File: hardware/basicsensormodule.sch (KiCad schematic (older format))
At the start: 6 parts, among them J1 Conn_01x04

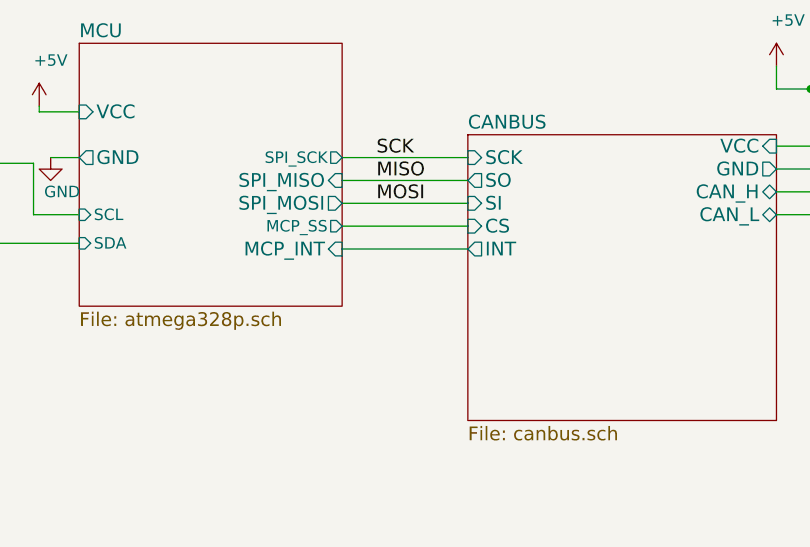
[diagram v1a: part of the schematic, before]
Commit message: Adicão da alimentação de uma folha para outra .
Alimentação de 3V3.
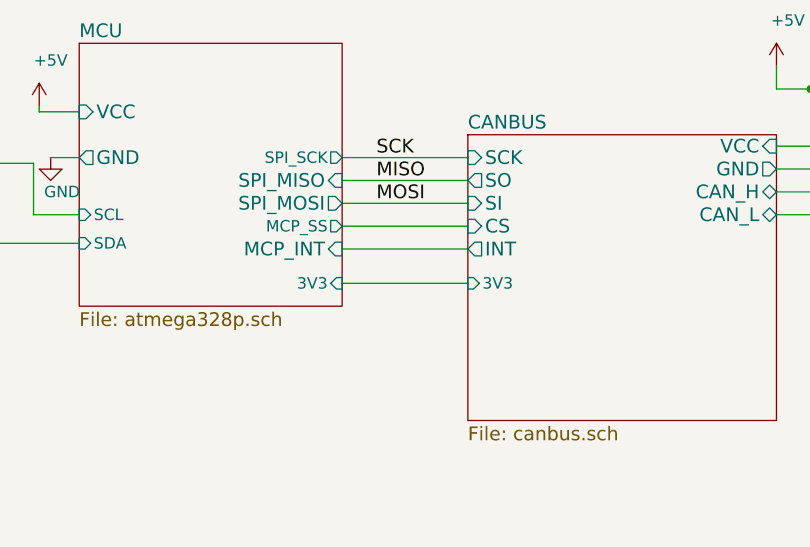
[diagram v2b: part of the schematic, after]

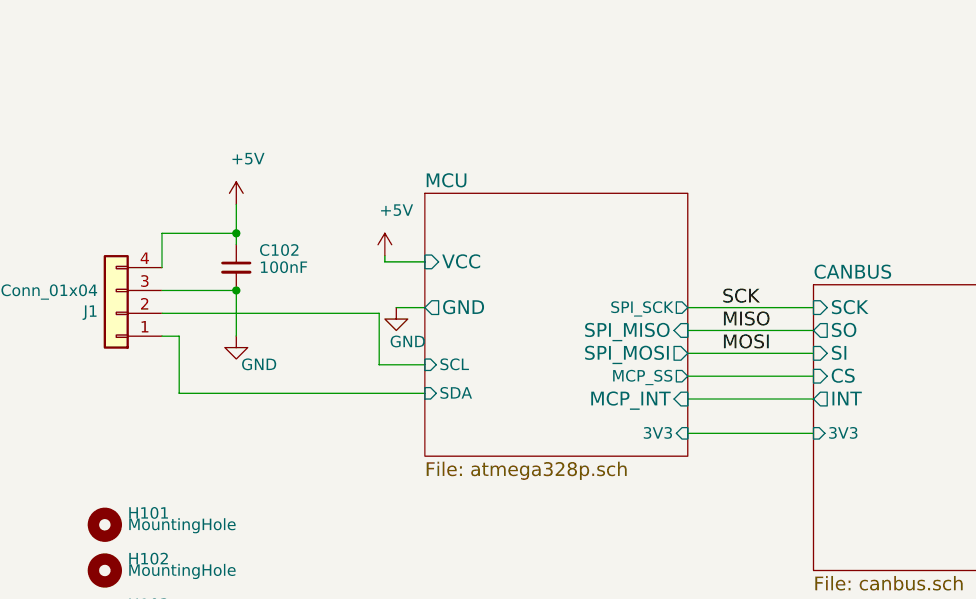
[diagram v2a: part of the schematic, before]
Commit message: PCB atualizada com as mudanças do raspberry
Foram adicionadas as mudanças do conector do raspberry e retirado algumas coisas não necessárias.
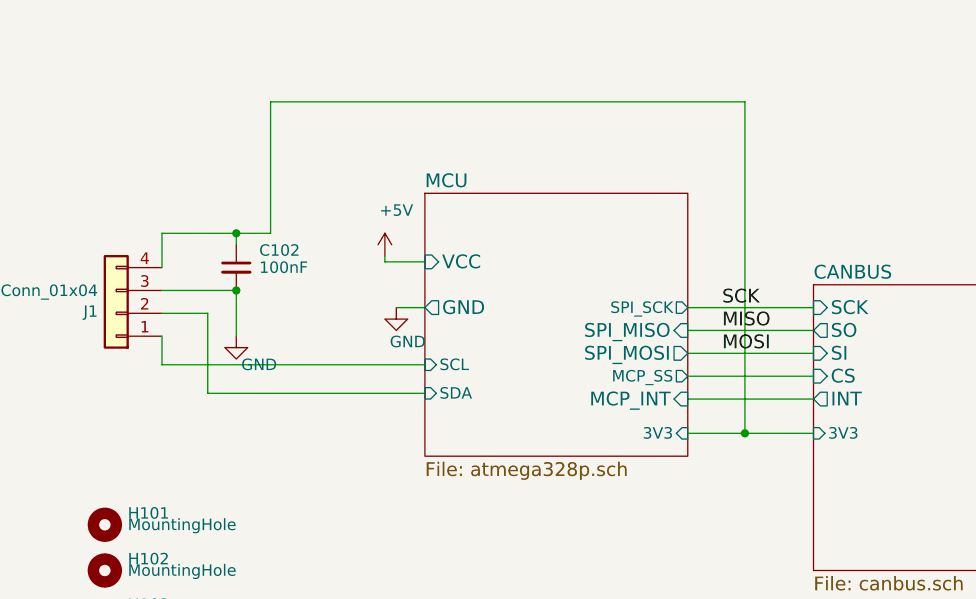
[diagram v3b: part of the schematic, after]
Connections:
- net +5V: no longer C102.1, J1.4 (Pin_4)
- net CANBUS/3V3: now also C102.1, J1.4 (Pin_4)
- net MCU/SCL: now also J1.1 (Pin_1); no longer J1.2 (Pin_2)
- net MCU/SDA: now also J1.2 (Pin_2); no longer J1.1 (Pin_1)
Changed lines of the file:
@@
-$EndComp
-$Comp
-L power:+5V #PWR0104
-U 1 1 5BE8FC8C
-P 3525 3650
-F 0 "#PWR0104" H 3525 3500 50  0001 C CNN
-F 1 "+5V" H 3575 3850 50  0000 C CNN
-F 2 "" H 3525 3650 50  0001 C CNN
-F 3 "" H 3525 3650 50  0001 C CNN
-	1    3525 3650
-	1    0    0    -1
 $EndComp
 $Comp
@@
 Wire Wire Line
 	3525 3775 3525 3825
-Wire Wire Line
-	3525 3650 3525 3775
 Connection ~ 3525 3775
 $Comp
@@
 Wire Wire Line
 	3200 3775 3525 3775
-Wire Wire Line
-	3200 4125 4150 4125
-Wire Wire Line
-	4150 4125 4150 4350
-Wire Wire Line
-	4150 4350 4350 4350
-Wire Wire Line
-	3275 4475 3275 4225
-Wire Wire Line
-	3275 4225 3200 4225
-Wire Wire Line
-	3275 4475 4350 4475
 Wire Wire Line
 	3525 4225 3525 4025
@@
 $EndSheet
 Wire Wire Line
-	6050 4650 5500 4650
+	6050 4650 5750 4650
+Wire Wire Line
+	5750 4650 5750 3200
+Wire Wire Line
+	5750 3200 3675 3200
+Wire Wire Line
+	3675 3200 3675 3775
+Wire Wire Line
+	3675 3775 3525 3775
+Connection ~ 5750 4650
+Wire Wire Line
+	5750 4650 5500 4650
+Wire Wire Line
+	3200 4125 3400 4125
+Wire Wire Line
+	3400 4125 3400 4475
+Wire Wire Line
+	3400 4475 4350 4475
+Wire Wire Line
+	3200 4225 3200 4350
+Wire Wire Line
+	3200 4350 4350 4350
 $EndSCHEMATC

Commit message: Project cleaned
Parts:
- added J401: USART, Connector_PinHeader_2.54mm:PinHeader_1x04_P2.54mm_Vertical, symbol Connector_Generic:Conn_01x04
- added R402, R403: 1k, Resistor_SMD:R_0805_2012Metric_Pad1.15x1.40mm_HandSolder, symbol Device:R_Small
- J1: value Conn_01x04 -> I2C
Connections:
- net GND: now also J401.1 (Pin_1)
- net CANBUS/3V3 renamed +3V3
- new net: J401.3 (Pin_3), R402.2
- new net: J401.2 (Pin_2), R403.2
- new net MCU/USART_RX: R402.1
- new net MCU/USART_TX: R403.1
- no-connect marks 0 -> 2
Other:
- moved on the sheet: C102, H101, H102, H103, H104, J1
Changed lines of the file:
@@
 	7550 3800 7550 4050
-$Comp
-L Device:C_Small C102
-U 1 1 5BE67608
-P 3525 3925
-F 0 "C102" H 3625 4000 50  0000 L CNN
-F 1 "100nF" H 3625 3925 50  0000 L CNN
-F 2 "Capacitor_SMD:C_0805_2012Metric_Pad1.15x1.40mm_HandSolder" H 3525 3925 50  0001 C CNN
-F 3 "~" H 3525 3925 50  0001 C CNN
-	1    3525 3925
-	1    0    0    -1
-$EndComp
 $Comp
 L basicsensormodule-rescue:MountingHole-Mechanical H104
 U 1 1 5BE9AF15
-P 2950 5650
-F 0 "H104" H 3050 5700 50  0000 L CNN
-F 1 "MountingHole" H 3050 5650 50  0000 L CNN
-F 2 "MountingHole:MountingHole_3.2mm_M3" H 2950 5650 50  0001 C CNN
-F 3 "~" H 2950 5650 50  0001 C CNN
-	1    2950 5650
+P 5700 6900
+F 0 "H104" H 5800 6950 50  0000 L CNN
+F 1 "MountingHole" H 5800 6900 50  0000 L CNN
+F 2 "MountingHole:MountingHole_3.2mm_M3" H 5700 6900 50  0001 C CNN
+F 3 "~" H 5700 6900 50  0001 C CNN
+	1    5700 6900
 	1    0    0    -1
 $EndComp
@@
 L basicsensormodule-rescue:MountingHole-Mechanical H103
 U 1 1 5BE9BC53
-P 2950 5450
-F 0 "H103" H 3050 5500 50  0000 L CNN
-F 1 "MountingHole" H 3050 5450 50  0000 L CNN
-F 2 "MountingHole:MountingHole_3.2mm_M3" H 2950 5450 50  0001 C CNN
-F 3 "~" H 2950 5450 50  0001 C CNN
-	1    2950 5450
+P 5700 6700
+F 0 "H103" H 5800 6750 50  0000 L CNN
+F 1 "MountingHole" H 5800 6700 50  0000 L CNN
+F 2 "MountingHole:MountingHole_3.2mm_M3" H 5700 6700 50  0001 C CNN
+F 3 "~" H 5700 6700 50  0001 C CNN
+	1    5700 6700
 	1    0    0    -1
 $EndComp
@@
 L basicsensormodule-rescue:MountingHole-Mechanical H102
 U 1 1 5BE9BC79
-P 2950 5250
-F 0 "H102" H 3050 5300 50  0000 L CNN
-F 1 "MountingHole" H 3050 5250 50  0000 L CNN
-F 2 "MountingHole:MountingHole_3.2mm_M3" H 2950 5250 50  0001 C CNN
-F 3 "~" H 2950 5250 50  0001 C CNN
-	1    2950 5250
+P 5700 6500
+F 0 "H102" H 5800 6550 50  0000 L CNN
+F 1 "MountingHole" H 5800 6500 50  0000 L CNN
+F 2 "MountingHole:MountingHole_3.2mm_M3" H 5700 6500 50  0001 C CNN
+F 3 "~" H 5700 6500 50  0001 C CNN
+	1    5700 6500
 	1    0    0    -1
 $EndComp
@@
 L basicsensormodule-rescue:MountingHole-Mechanical H101
 U 1 1 5BE9BC9F
-P 2950 5050
-F 0 "H101" H 3050 5100 50  0000 L CNN
-F 1 "MountingHole" H 3050 5050 50  0000 L CNN
-F 2 "MountingHole:MountingHole_3.2mm_M3" H 2950 5050 50  0001 C CNN
-F 3 "~" H 2950 5050 50  0001 C CNN
-	1    2950 5050
+P 5700 6300
+F 0 "H101" H 5800 6350 50  0000 L CNN
+F 1 "MountingHole" H 5800 6300 50  0000 L CNN
+F 2 "MountingHole:MountingHole_3.2mm_M3" H 5700 6300 50  0001 C CNN
+F 3 "~" H 5700 6300 50  0001 C CNN
+	1    5700 6300
 	1    0    0    -1
 $EndComp
@@
 $EndComp
 $Comp
-L Connector_Generic:Conn_01x04 J1
-U 1 1 5CB1A26C
-P 3000 4125
-F 0 "J1" H 3080 4117 50  0000 L CNN
-F 1 "Conn_01x04" H 3080 4026 50  0000 L CNN
-F 2 "Connector_PinHeader_2.54mm:PinHeader_1x04_P2.54mm_Vertical" H 3000 4125 50  0001 C CNN
-F 3 "~" H 3000 4125 50  0001 C CNN
-	1    3000 4125
-	-1   0    0    1
-$EndComp
-Wire Wire Line
-	3525 3775 3525 3825
-Connection ~ 3525 3775
-$Comp
-L power:GND #PWR0101
-U 1 1 5BE8F6F0
-P 3525 4225
-F 0 "#PWR0101" H 3525 3975 50  0001 C CNN
-F 1 "GND" H 3625 4100 50  0000 C CNN
-F 2 "" H 3525 4225 50  0001 C CNN
-F 3 "" H 3525 4225 50  0001 C CNN
-	1    3525 4225
-	1    0    0    -1
-$EndComp
-Wire Wire Line
-	3200 4025 3525 4025
-Wire Wire Line
-	3200 3775 3200 3925
-Wire Wire Line
-	3200 3775 3525 3775
-Wire Wire Line
-	3525 4225 3525 4025
-Connection ~ 3525 4025
-$Comp
 L power:+5V #PWR0102
 U 1 1 5CB14A9F
@@
 Wire Wire Line
 	4175 3900 4175 3875
+$Comp
+L power:GND #PWR0101
+U 1 1 5BE8F6F0
+P 3300 4650
+F 0 "#PWR0101" H 3300 4400 50  0001 C CNN
+F 1 "GND" H 3400 4525 50  0000 C CNN
+F 2 "" H 3300 4650 50  0001 C CNN
+F 3 "" H 3300 4650 50  0001 C CNN
+	1    3300 4650
+	1    0    0    -1
+$EndComp
+$Comp
+L Device:R_Small R?
+U 1 1 5D49B5FD
+P 3400 5100
+AR Path="/5AACA401/5D49B5FD" Ref="R?"  Part="1"
+AR Path="/5D49B5FD" Ref="R403"  Part="1"
+F 0 "R403" V 3450 5200 50  0000 L CNN
+F 1 "1k" V 3450 4950 50  0000 L CNN
+F 2 "Resistor_SMD:R_0805_2012Metric_Pad1.15x1.40mm_HandSolder" H 3400 5100 50  0001 C CNN
+F 3 "" H 3400 5100 50  0001 C CNN
+	1    3400 5100
+	0    1    -1   0
+$EndComp
+Wire Wire Line
+	3300 5100 3200 5100
+$Comp
+L power:GND #PWR?
+U 1 1 5D49B5F6
+P 3300 5300
+AR Path="/5AACA401/5D49B5F6" Ref="#PWR?"  Part="1"
+AR Path="/5D49B5F6" Ref="#PWR?"  Part="1"
+F 0 "#PWR?" H 3300 5050 50  0001 C CNN
+F 1 "GND" H 3350 5100 50  0000 C CNN
+F 2 "" H 3300 5300 50  0001 C CNN
+F 3 "" H 3300 5300 50  0001 C CNN
+	1    3300 5300
+	-1   0    0    -1
+$EndComp
+Wire Wire Line
+	3300 5300 3300 5200
+Wire Wire Line
+	3300 5200 3200 5200
+Wire Wire Line
+	3300 5000 3200 5000
+$Comp
+L Device:R_Small R?
+U 1 1 5D49B5E3
+P 3400 5000
+AR Path="/5AACA401/5D49B5E3" Ref="R?"  Part="1"
+AR Path="/5D49B5E3" Ref="R402"  Part="1"
+F 0 "R402" V 3450 5100 50  0000 L CNN
+F 1 "1k" V 3450 4850 50  0000 L CNN
+F 2 "Resistor_SMD:R_0805_2012Metric_Pad1.15x1.40mm_HandSolder" H 3400 5000 50  0001 C CNN
+F 3 "" H 3400 5000 50  0001 C CNN
+	1    3400 5000
+	0    1    -1   0
+$EndComp
+NoConn ~ 3200 4900
+Wire Wire Line
+	3750 4600 3750 5000
+Wire Wire Line
+	3750 5000 3500 5000
+Wire Wire Line
+	3750 4600 4350 4600
+Wire Wire Line
+	4350 4700 3850 4700
+Wire Wire Line
+	3850 4700 3850 5100
+Wire Wire Line
+	3850 5100 3500 5100
 $Sheet
 S 4350 3600 1150 1150
@@
 F7 "SPI_SCK" O R 5500 4100 50
 F8 "MCP_SS" O R 5500 4400 50
-F9 "SCL" I L 4350 4350 50
-F10 "SDA" I L 4350 4475 50
+F9 "SCL" I L 4350 4500 50
+F10 "SDA" I L 4350 4400 50
 F11 "3V3" I R 5500 4650 50
+F12 "USART_TX" I L 4350 4700 50
+F13 "USART_RX" I L 4350 4600 50
 $EndSheet
-Wire Wire Line
-	6050 4650 5750 4650
-Wire Wire Line
-	5750 4650 5750 3200
-Wire Wire Line
-	5750 3200 3675 3200
-Wire Wire Line
-	3675 3200 3675 3775
-Wire Wire Line
-	3675 3775 3525 3775
-Connection ~ 5750 4650
-Wire Wire Line
-	5750 4650 5500 4650
-Wire Wire Line
-	3200 4125 3400 4125
-Wire Wire Line
-	3400 4125 3400 4475
-Wire Wire Line
-	3400 4475 4350 4475
-Wire Wire Line
-	3200 4225 3200 4350
-Wire Wire Line
-	3200 4350 4350 4350
+$Comp
+L Connector_Generic:Conn_01x04 J?
+U 1 1 5D49B5EA
+P 3000 5100
+AR Path="/5AACA401/5D49B5EA" Ref="J?"  Part="1"
+AR Path="/5D49B5EA" Ref="J401"  Part="1"
+F 0 "J401" H 3200 4950 50  0000 C CNN
+F 1 "USART" H 3250 5100 50  0000 C CNN
+F 2 "Connector_PinHeader_2.54mm:PinHeader_1x04_P2.54mm_Vertical" H 3000 5100 50  0001 C CNN
+F 3 "~" H 3000 5100 50  0001 C CNN
+	1    3000 5100
+	-1   0    0    1
+$EndComp
+$Comp
+L Connector_Generic:Conn_01x04 J1
+U 1 1 5CB1A26C
+P 3000 4400
+F 0 "J1" H 3080 4392 50  0000 L CNN
+F 1 "I2C" H 3080 4301 50  0000 L CNN
+F 2 "Connector_PinHeader_2.54mm:PinHeader_1x04_P2.54mm_Vertical" H 3000 4400 50  0001 C CNN
+F 3 "~" H 3000 4400 50  0001 C CNN
+	1    3000 4400
+	-1   0    0    1
+$EndComp
+Wire Wire Line
+	3200 4500 4350 4500
+Wire Wire Line
+	3300 4300 3200 4300
+Wire Wire Line
+	3300 4650 3300 4600
+Wire Wire Line
+	4350 4400 3200 4400
+$Comp
+L Device:C_Small C102
+U 1 1 5BE67608
+P 3450 4450
+F 0 "C102" H 3550 4525 50  0000 L CNN
+F 1 "100nF" H 3550 4450 50  0000 L CNN
+F 2 "Capacitor_SMD:C_0805_2012Metric_Pad1.15x1.40mm_HandSolder" H 3450 4450 50  0001 C CNN
+F 3 "~" H 3450 4450 50  0001 C CNN
+	1    3450 4450
+	1    0    0    -1
+$EndComp
+Wire Wire Line
+	3450 4550 3450 4600
+Wire Wire Line
+	3450 4600 3300 4600
+Connection ~ 3300 4600
+Wire Wire Line
+	3300 4600 3300 4300
+Wire Wire Line
+	3450 4350 3450 4200
+Wire Wire Line
+	3450 4200 3200 4200
+Wire Wire Line
+	3450 4150 3450 4200
+Connection ~ 3450 4200
+Wire Wire Line
+	5500 4650 5650 4650
+$Comp
+L power:+3V3 #PWR?
+U 1 1 5D4C7974
+P 5650 4650
+F 0 "#PWR?" H 5650 4500 50  0001 C CNN
+F 1 "+3V3" H 5750 4750 50  0000 C CNN
+F 2 "" H 5650 4650 50  0001 C CNN
+F 3 "" H 5650 4650 50  0001 C CNN
+	1    5650 4650
+	1    0    0    -1
+$EndComp
+Connection ~ 5650 4650
+Wire Wire Line
+	5650 4650 6050 4650
+$Comp
+L power:+3V3 #PWR?
+U 1 1 5D4C8498
+P 3450 4150
+F 0 "#PWR?" H 3450 4000 50  0001 C CNN
+F 1 "+3V3" H 3450 4350 50  0000 C CNN
+F 2 "" H 3450 4150 50  0001 C CNN
+F 3 "" H 3450 4150 50  0001 C CNN
+	1    3450 4150
+	1    0    0    -1
+$EndComp
+NoConn ~ 7750 3150
 $EndSCHEMATC
